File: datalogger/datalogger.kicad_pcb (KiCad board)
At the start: 4 copper layers, 30 x 42 mm, 42 parts, among them J1 MSD-1-A, J2 USB4216-03-A_REVA, Q1 NPN, Q2 NPN, U1 BME280, U2 CP2102N-Axx-xQFN28, U3 ESP32-C3-MINI-1-N4, U4 TLV76133DCYR

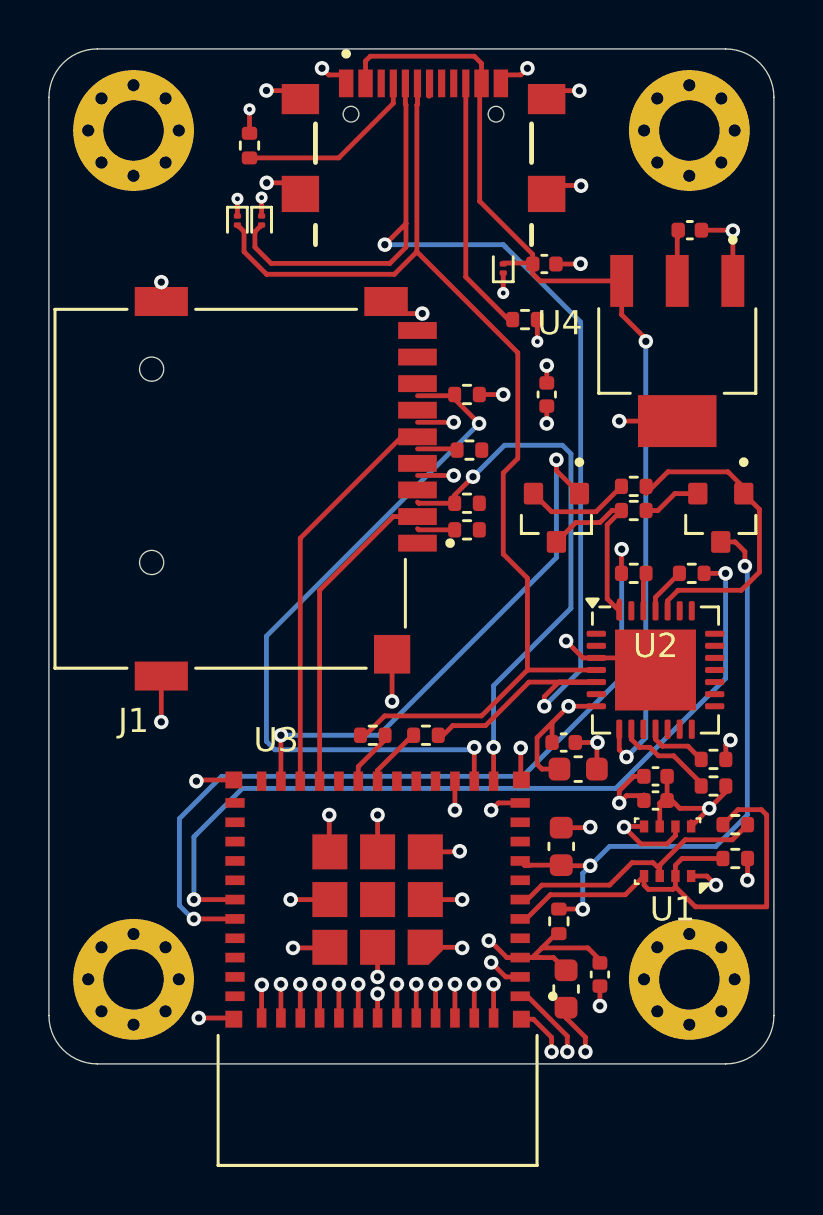
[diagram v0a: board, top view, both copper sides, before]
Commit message: Change USB-C orientation
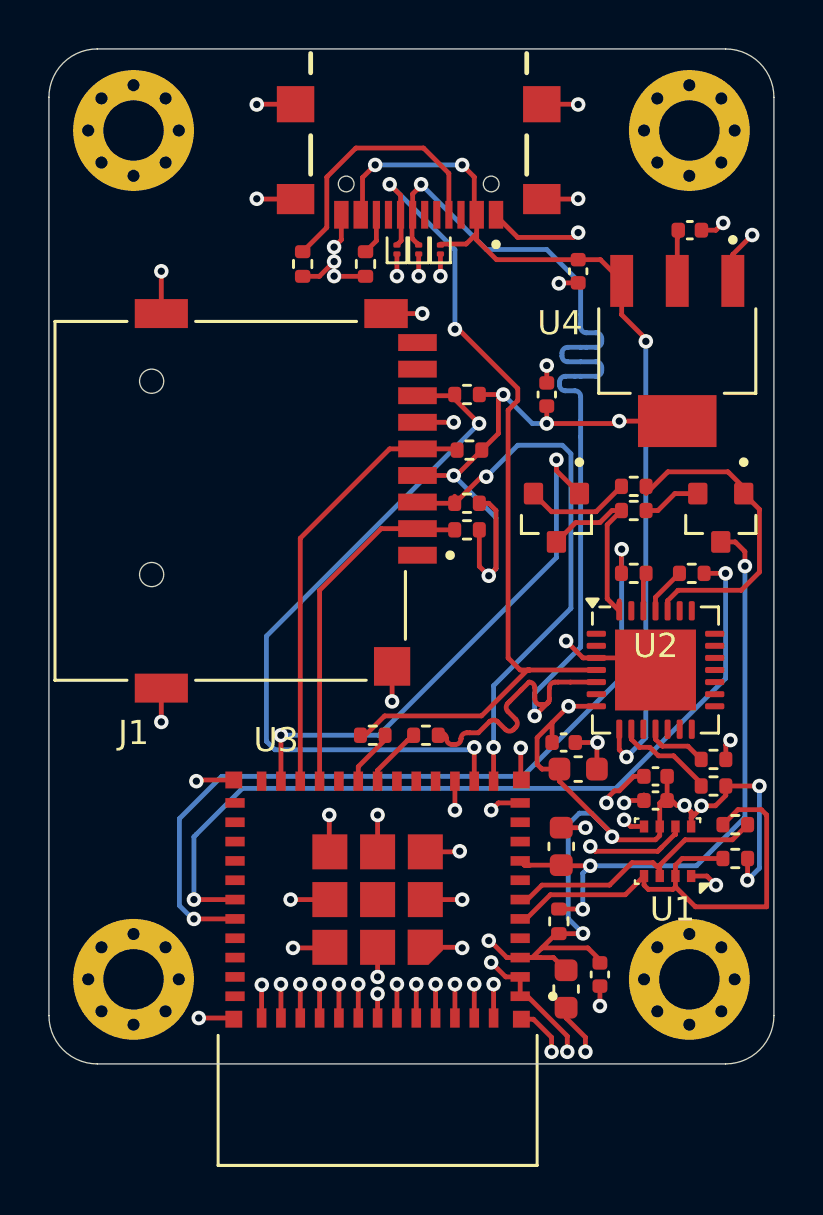
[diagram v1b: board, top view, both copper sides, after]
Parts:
- moved R1 6.99 mm to (158.1, 58.4), turned to -90 degrees
- moved D1 6.71 mm to (159.4, 57.8), turned to 90 degrees
- moved D2 6.61 mm to (160.3, 57.8), turned to 90 degrees
- moved R10 5.37 mm to (155.5, 58.4), turned to -90 degrees
- moved D3 2.72 mm to (161.2, 57.8)
- moved C3 1.43 mm to (166.9, 58.7), turned to -90 degrees
- moved J2 1.43 mm to (160.3, 52.9), turned to 180 degrees
- moved J1 0.50 mm to (152.5, 68.2)
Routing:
- net +3V3: track 30.8 -> 70.9 mm, vias 8 -> 13
- net U2_D+: track 47.0 -> 36.9 mm, vias 0 -> 2
- net Net-(J2-CC2): track 10.6 -> 1.71 mm
- net GNDREF: track 87.8 -> 95.3 mm, vias 57 -> 60
- net U2_D-: track 52.3 -> 47.0 mm
- net Net-(J2-CC1): track 7.71 -> 11.2 mm
- net +5V: track 42.6 -> 39.4 mm, vias 2 -> 4
- removed copper zone on In2.Cu, net +3V3
